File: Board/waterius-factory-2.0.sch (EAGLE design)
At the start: 24 parts, among them IC1 TINY13-20SU, U3 ESP01

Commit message: correct Board 2.0
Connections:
- net GND1: now also S1.S; no longer S1.P
- net SCK: now also S1.P; no longer S1.S
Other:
- moved on the sheet: S1
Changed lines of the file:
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@@
 <?xml version="1.0" encoding="utf-8"?>
 <!DOCTYPE eagle SYSTEM "eagle.dtd">
-<eagle version="9.0.0">
+<eagle version="9.0.1">
 <drawing>
 <settings>
@@
 <grid distance="0.1" unitdist="inch" unit="inch" style="lines" multiple="1" display="no" altdistance="0.01" altunitdist="inch" altunit="inch"/>
 <layers>
-<layer number="1" name="Top" color="4" fill="1" visible="yes" active="no"/>
-<layer number="2" name="Route2" color="1" fill="3" visible="yes" active="no"/>
-<layer number="3" name="Route3" color="4" fill="3" visible="yes" active="no"/>
-<layer number="4" name="Route4" color="1" fill="4" visible="yes" active="no"/>
-<layer number="5" name="Route5" color="4" fill="4" visible="yes" active="no"/>
-<layer number="6" name="Route6" color="1" fill="8" visible="yes" active="no"/>
-<layer number="7" name="Route7" color="4" fill="8" visible="yes" active="no"/>
-<layer number="8" name="Route8" color="1" fill="2" visible="yes" active="no"/>
-<layer number="9" name="Route9" color="4" fill="2" visible="yes" active="no"/>
-<layer number="10" name="Route10" color="1" fill="7" visible="yes" active="no"/>
-<layer number="11" name="Route11" color="4" fill="7" visible="yes" active="no"/>
-<layer number="12" name="Route12" color="1" fill="5" visible="yes" active="no"/>
-<layer number="13" name="Route13" color="4" fill="5" visible="yes" active="no"/>
-<layer number="14" name="Route14" color="1" fill="6" visible="yes" active="no"/>
-<layer number="15" name="Route15" color="4" fill="6" visible="yes" active="no"/>
-<layer number="16" name="Bottom" color="1" fill="1" visible="yes" active="no"/>
-<layer number="17" name="Pads" color="2" fill="1" visible="yes" active="no"/>
-<layer number="18" name="Vias" color="2" fill="1" visible="yes" active="no"/>
-<layer number="19" name="Unrouted" color="6" fill="1" visible="yes" active="no"/>
-<layer number="20" name="Dimension" color="24" fill="1" visible="yes" active="no"/>
-<layer number="21" name="tPlace" color="7" fill="1" visible="yes" active="no"/>
-<layer number="22" name="bPlace" color="7" fill="1" visible="yes" active="no"/>
-<layer number="23" name="tOrigins" color="15" fill="1" visible="yes" active="no"/>
-<layer number="24" name="bOrigins" color="15" fill="1" visible="yes" active="no"/>
-<layer number="25" name="tNames" color="7" fill="1" visible="yes" active="no"/>
-<layer number="26" name="bNames" color="7" fill="1" visible="yes" active="no"/>
-<layer number="27" name="tValues" color="7" fill="1" visible="yes" active="no"/>
-<layer number="28" name="bValues" color="7" fill="1" visible="yes" active="no"/>
+<layer number="1" name="Top" color="4" fill="1" visible="no" active="no"/>
+<layer number="2" name="Route2" color="1" fill="3" visible="no" active="no"/>
+<layer number="3" name="Route3" color="4" fill="3" visible="no" active="no"/>
+<layer number="4" name="Route4" color="1" fill="4" visible="no" active="no"/>
+<layer number="5" name="Route5" color="4" fill="4" visible="no" active="no"/>
+<layer number="6" name="Route6" color="1" fill="8" visible="no" active="no"/>
+<layer number="7" name="Route7" color="4" fill="8" visible="no" active="no"/>
+<layer number="8" name="Route8" color="1" fill="2" visible="no" active="no"/>
+<layer number="9" name="Route9" color="4" fill="2" visible="no" active="no"/>
+<layer number="10" name="Route10" color="1" fill="7" visible="no" active="no"/>
+<layer number="11" name="Route11" color="4" fill="7" visible="no" active="no"/>
+<layer number="12" name="Route12" color="1" fill="5" visible="no" active="no"/>
+<layer number="13" name="Route13" color="4" fill="5" visible="no" active="no"/>
+<layer number="14" name="Route14" color="1" fill="6" visible="no" active="no"/>
+<layer number="15" name="Route15" color="4" fill="6" visible="no" active="no"/>
+<layer number="16" name="Bottom" color="1" fill="1" visible="no" active="no"/>
+<layer number="17" name="Pads" color="2" fill="1" visible="no" active="no"/>
+<layer number="18" name="Vias" color="2" fill="1" visible="no" active="no"/>
+<layer number="19" name="Unrouted" color="6" fill="1" visible="no" active="no"/>
+<layer number="20" name="Dimension" color="24" fill="1" visible="no" active="no"/>
+<layer number="21" name="tPlace" color="7" fill="1" visible="no" active="no"/>
+<layer number="22" name="bPlace" color="7" fill="1" visible="no" active="no"/>
+<layer number="23" name="tOrigins" color="15" fill="1" visible="no" active="no"/>
+<layer number="24" name="bOrigins" color="15" fill="1" visible="no" active="no"/>
+<layer number="25" name="tNames" color="7" fill="1" visible="no" active="no"/>
+<layer number="26" name="bNames" color="7" fill="1" visible="no" active="no"/>
+<layer number="27" name="tValues" color="7" fill="1" visible="no" active="no"/>
+<layer number="28" name="bValues" color="7" fill="1" visible="no" active="no"/>
 <layer number="29" name="tStop" color="7" fill="3" visible="no" active="no"/>
 <layer number="30" name="bStop" color="7" fill="6" visible="no" active="no"/>
@@
 <layer number="35" name="tGlue" color="7" fill="4" visible="no" active="no"/>
 <layer number="36" name="bGlue" color="7" fill="5" visible="no" active="no"/>
-<layer number="37" name="tTest" color="7" fill="1" visible="yes" active="no"/>
-<layer number="38" name="bTest" color="7" fill="1" visible="yes" active="no"/>
+<layer number="37" name="tTest" color="7" fill="1" visible="no" active="no"/>
+<layer number="38" name="bTest" color="7" fill="1" visible="no" active="no"/>
 <layer number="39" name="tKeepout" color="4" fill="11" visible="no" active="no"/>
 <layer number="40" name="bKeepout" color="1" fill="11" visible="no" active="no"/>
@@
 <layer number="44" name="Drills" color="7" fill="1" visible="no" active="no"/>
 <layer number="45" name="Holes" color="7" fill="1" visible="no" active="no"/>
-<layer number="46" name="Milling" color="3" fill="1" visible="yes" active="no"/>
-<layer number="47" name="Measures" color="7" fill="1" visible="yes" active="no"/>
-<layer number="48" name="Document" color="7" fill="1" visible="yes" active="no"/>
-<layer number="49" name="Reference" color="7" fill="1" visible="yes" active="no"/>
-<layer number="51" name="tDocu" color="7" fill="1" visible="yes" active="no"/>
-<layer number="52" name="bDocu" color="7" fill="1" visible="yes" active="no"/>
+<layer number="46" name="Milling" color="3" fill="1" visible="no" active="no"/>
+<layer number="47" name="Measures" color="7" fill="1" visible="no" active="no"/>
+<layer number="48" name="Document" color="7" fill="1" visible="no" active="no"/>
+<layer number="49" name="Reference" color="7" fill="1" visible="no" active="no"/>
+<layer number="51" name="tDocu" color="7" fill="1" visible="no" active="no"/>
+<layer number="52" name="bDocu" color="7" fill="1" visible="no" active="no"/>
 <layer number="88" name="SimResults" color="9" fill="1" visible="yes" active="yes"/>
 <layer number="89" name="SimProbes" color="9" fill="1" visible="yes" active="yes"/>
@@
 <instance part="R10" gate="G$1" x="-22.86" y="15.24" rot="R90"/>
 <instance part="GND6" gate="1" x="-22.86" y="7.62"/>
-<instance part="S1" gate="1" x="43.18" y="25.4"/>
+<instance part="S1" gate="1" x="43.18" y="25.4" rot="MR180"/>
 </instances>
 <busses>
@@
 </segment>
 <segment>
+<label x="43.18" y="17.78" size="1.778" layer="95"/>
 <wire x1="43.18" y1="17.78" x2="43.18" y2="20.32" width="0.1524" layer="91"/>
-<label x="43.18" y="17.78" size="1.778" layer="95"/>
-<pinref part="S1" gate="1" pin="P"/>
+<pinref part="S1" gate="1" pin="S"/>
 </segment>
 </net>
@@
 <pinref part="U3" gate="G$1" pin="GPIO2"/>
 <label x="48.26" y="35.56" size="1.778" layer="95"/>
-<wire x1="43.18" y1="35.56" x2="43.18" y2="30.48" width="0.1524" layer="91"/>
-<pinref part="S1" gate="1" pin="S"/>
-</segment>
-<segment>
+<pinref part="S1" gate="1" pin="P"/>
+<wire x1="43.18" y1="30.48" x2="43.18" y2="35.56" width="0.1524" layer="91"/>
+</segment>
+<segment>

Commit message: board correct, https://github.com/dontsovcmc/waterius/issues/87
remove 47k untested resister
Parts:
- removed R10: 47к, resistor:R-EU_R0805
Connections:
- net GND: no longer R10.1
- net N$5: no longer R10.2
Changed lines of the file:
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@@
 <?xml version="1.0" encoding="utf-8"?>
 <!DOCTYPE eagle SYSTEM "eagle.dtd">
-<eagle version="9.0.1">
+<eagle version="9.0.0">
 <drawing>
 <settings>
@@
 <part name="GND7" library="supply1" deviceset="GND" device=""/>
 <part name="U$1" library="Microchip_By_element14_Batch_1" deviceset="MCP1700T-3002E/TT" device=""/>
-<part name="R10" library="resistor" deviceset="R-EU_" device="R0805" value="47к"/>
-<part name="GND6" library="supply1" deviceset="GND" device=""/>
 <part name="S1" library="switch-omron" library_urn="urn:adsk.eagle:library:377" deviceset="31-XX" device="" package3d_urn="urn:adsk.eagle:package:27487/1"/>
 </parts>
@@
 <instance part="GND7" gate="1" x="76.2" y="2.54"/>
 <instance part="U$1" gate="A" x="17.78" y="96.52"/>
-<instance part="R10" gate="G$1" x="-22.86" y="15.24" rot="R90"/>
-<instance part="GND6" gate="1" x="-22.86" y="7.62"/>
 <instance part="S1" gate="1" x="43.18" y="25.4" rot="MR180"/>
 </instances>
@@
 <junction x="76.2" y="7.62"/>
 </segment>
-<segment>
-<pinref part="R10" gate="G$1" pin="1"/>
-<pinref part="GND6" gate="1" pin="GND"/>
-</segment>
 </net>
 <net name="N$3" class="0">
@@
 <pinref part="U3" gate="G$1" pin="TXD"/>
 <pinref part="LOG" gate="G$1" pin="1"/>
-<wire x1="-5.08" y1="33.02" x2="-22.86" y2="33.02" width="0.1524" layer="91"/>
-<wire x1="-22.86" y1="33.02" x2="-33.02" y2="33.02" width="0.1524" layer="91"/>
+<wire x1="-5.08" y1="33.02" x2="-33.02" y2="33.02" width="0.1524" layer="91"/>
 <wire x1="-33.02" y1="33.02" x2="-33.02" y2="45.72" width="0.1524" layer="91"/>
 <pinref part="LED1" gate="G$1" pin="A"/>
 <wire x1="-33.02" y1="30.48" x2="-33.02" y2="33.02" width="0.1524" layer="91"/>
 <junction x="-33.02" y="33.02"/>
-<pinref part="R10" gate="G$1" pin="2"/>
-<wire x1="-22.86" y1="20.32" x2="-22.86" y2="33.02" width="0.1524" layer="91"/>
-<junction x="-22.86" y="33.02"/>
-</segment>
-</net>
+</segment>
+</net>

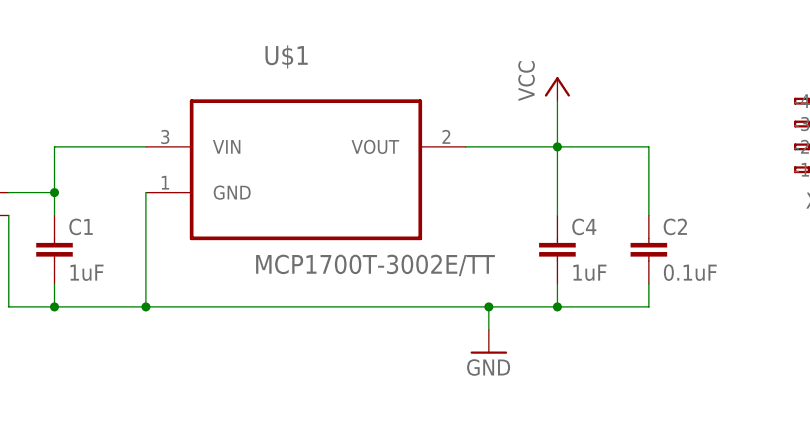
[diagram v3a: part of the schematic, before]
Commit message: replace mcp1700 file
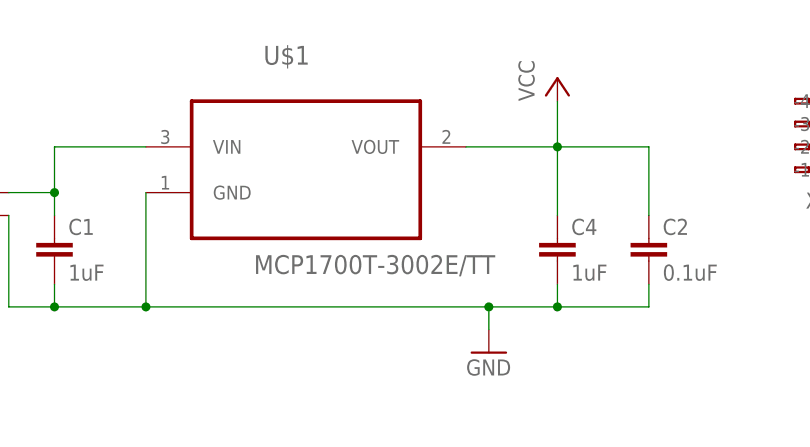
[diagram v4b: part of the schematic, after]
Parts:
- U$1: device Microchip_By_element14_Batch_1:MCP1700T-3002E/TT -> MCP1700T-3002E_TT:MCP1700T-3002E/TT
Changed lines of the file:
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@@
 <?xml version="1.0" encoding="utf-8"?>
 <!DOCTYPE eagle SYSTEM "eagle.dtd">
-<eagle version="9.0.1">
+<eagle version="9.0.0">
 <drawing>
 <settings>
@@
 <part name="C3" library="rcl" deviceset="C-EU" device="C0805" value="0.1uF"/>
 <part name="GND7" library="supply1" deviceset="GND" device=""/>
-<part name="U$1" library="Microchip_By_element14_Batch_1" deviceset="MCP1700T-3002E/TT" device=""/>
+<part name="U$1" library="MCP1700T-3002E_TT" deviceset="MCP1700T-3002E/TT" device=""/>
 <part name="S1" library="switch-omron" library_urn="urn:adsk.eagle:library:377" deviceset="31-XX" device="" package3d_urn="urn:adsk.eagle:package:27487/1"/>
 </parts>

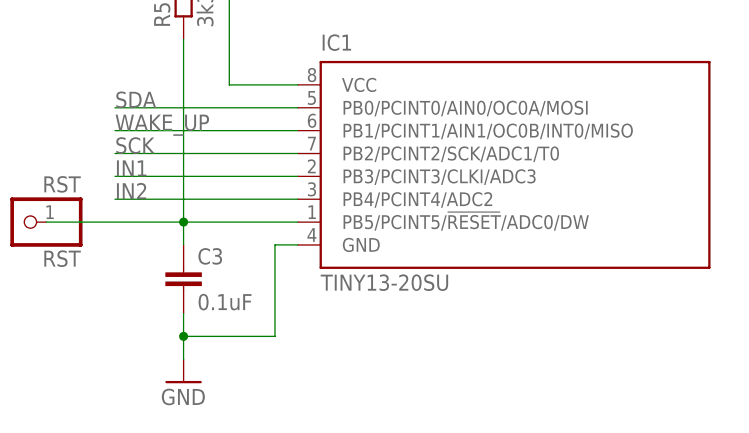
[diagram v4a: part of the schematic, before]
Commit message: attiny85 on sch
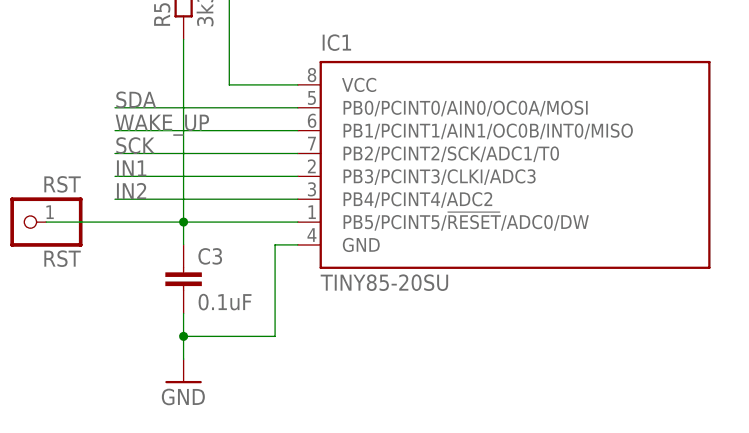
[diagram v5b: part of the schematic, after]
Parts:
- IC1: value TINY13-20SU -> TINY85-20SU
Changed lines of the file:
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@@
 <?xml version="1.0" encoding="utf-8"?>
 <!DOCTYPE eagle SYSTEM "eagle.dtd">
-<eagle version="9.0.0">
+<eagle version="9.0.1">
 <drawing>
 <settings>
@@
 <part name="GND5" library="supply1" deviceset="GND" device=""/>
 <part name="RST" library="pinhead" deviceset="PINHD-1X1" device="" value="RST"/>
-<part name="IC1" library="atmel" deviceset="TINY13" device="SU" technology="-20"/>
+<part name="IC1" library="atmel" deviceset="TINY13" device="SU" technology="-20" value="TINY85-20SU"/>
 <part name="R5" library="resistor" deviceset="R-EU_" device="R0805" value="3k3"/>
 <part name="C3" library="rcl" deviceset="C-EU" device="C0805" value="0.1uF"/>
